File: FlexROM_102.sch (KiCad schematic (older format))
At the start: 5 parts, among them J1 27C256 DIP LEGS, U1 28C256

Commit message: footprint name changed
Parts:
- J1: footprint 000_LOCAL:DIP-28_W15.24mm_pcb_sil_pins -> 000_LOCAL:DIP28_0.6_pcb_sil_pins
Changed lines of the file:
@@
 F 0 "J1" H 4440 4190 50  0000 C CNN
 F 1 "27C256 DIP LEGS" H 4260 4420 50  0000 C CNN
-F 2 "000_LOCAL:DIP-28_W15.24mm_pcb_sil_pins" H 4260 3040 50  0001 C CNN
+F 2 "000_LOCAL:DIP28_0.6_pcb_sil_pins" H 4260 3040 50  0001 C CNN
 F 3 "http://ww1.microchip.com/downloads/en/DeviceDoc/doc0014.pdf" H 4260 3040 50  0001 C CNN
 	1    4260 3040

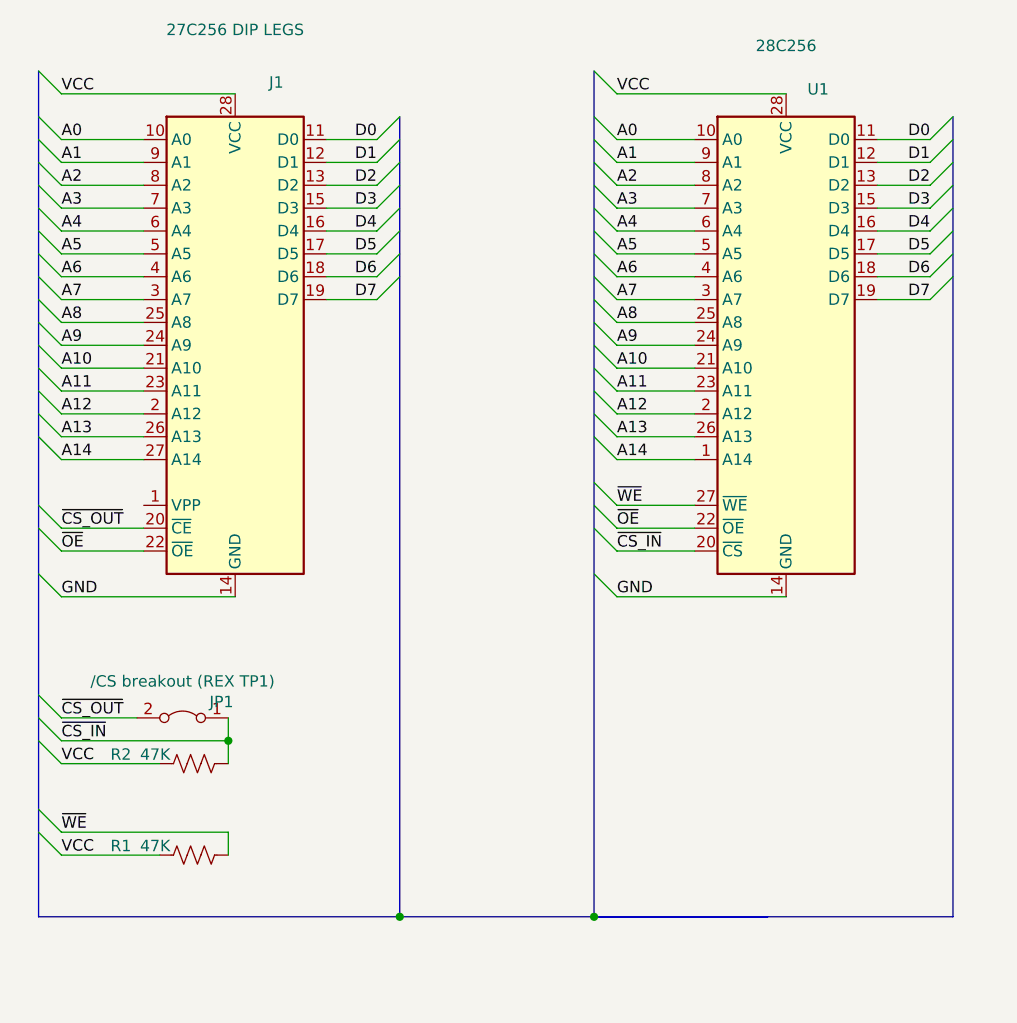
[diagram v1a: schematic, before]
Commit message: FlexROM_100 programming adapter, FlexROM_102 programming jumpers
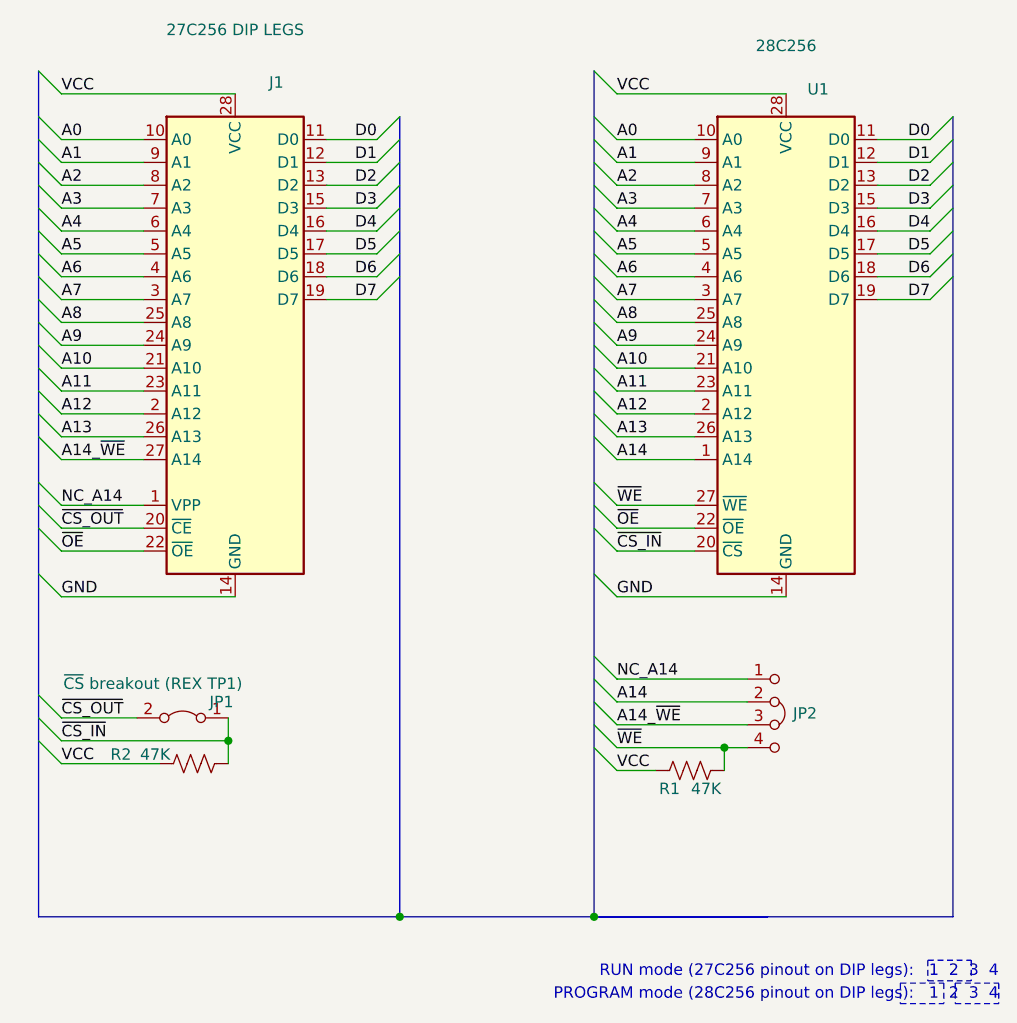
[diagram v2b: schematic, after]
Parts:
- added JP2: Jumper_4_Bridged23, Connector_PinHeader_2.00mm:PinHeader_1x04_P2.00mm_Horizontal, symbol 000_LOCAL:Jumper_4_Bridged23
- JP1: value /CS breakout (REX TP1) -> ~CS~ breakout (REX TP1)
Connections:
- net A14: now also JP2.2 (B); no longer J1.27 (A14)
- net ~WE: now also JP2.4 (D)
- net NC_A14: now reaches J1.1 (VPP)
- net NC_A14: now also JP2.1 (A)
- new net A14_~WE: J1.27 (A14), JP2.3 (C)
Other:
- note added: "PROGRAM mode (28C256 pinout on DIP legs): 1 2 3 4"
- note added: "RUN mode (27C256 pinout on DIP legs): 1 2 3 4"
- moved on the sheet: R1
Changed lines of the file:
@@
 A13
 Text Label 3500 3540 0    50   ~ 0
-A14
+A14_~WE
 Text Label 5930 2140 0    50   ~ 0
 A0
@@
 P 4030 4670
 F 0 "JP1" H 3860 4740 50  0000 C CNN
-F 1 "/CS breakout (REX TP1)" H 4030 4830 50  0000 C CNN
+F 1 "~CS~ breakout (REX TP1)" H 4160 4820 50  0000 C CNN
 F 2 "000_LOCAL:Pin_Header_Angled_1x02_Pitch2.54mm" H 4030 4670 50  0001 C CNN
 F 3 "~" H 4030 4670 50  0001 C CNN
@@
 Wire Bus Line
 	5830 5540 7400 5540
-Entry Wire Line
-	3400 5070 3500 5170
-Entry Wire Line
-	3400 5170 3500 5270
 $Comp
 L 000_LOCAL:R_US R1
 U 1 1 5E6B3AF8
-P 4080 5270
-F 0 "R1" V 4040 4950 50  0000 C CNN
-F 1 "47K" V 4040 5100 50  0000 C CNN
-F 2 "000_LOCAL:R_0805" H 4080 5270 50  0001 C CNN
-F 3 "~" H 4080 5270 50  0001 C CNN
-	1    4080 5270
+P 6250 4900
+F 0 "R1" V 6330 4810 50  0000 C CNN
+F 1 "47K" V 6330 4970 50  0000 C CNN
+F 2 "000_LOCAL:R_0805" H 6250 4900 50  0001 C CNN
+F 3 "~" H 6250 4900 50  0001 C CNN
+	1    6250 4900
 	0    1    1    0
 $EndComp
-Wire Wire Line
-	3500 5270 3930 5270
-Text Label 3500 5270 0    50   ~ 0
+Text Label 5930 4900 0    50   ~ 0
 VCC
-Text Label 3500 5170 0    50   ~ 0
+Text Label 5930 4800 0    50   ~ 0
 ~WE
 Connection ~ 4980 5540
@@
 Wire Wire Line
 	4230 4770 4230 4870
-Wire Wire Line
-	4230 5270 4230 5170
-Wire Wire Line
-	3500 5170 4230 5170
+Entry Wire Line
+	3400 3640 3500 3740
+Wire Wire Line
+	3860 3740 3500 3740
+Text Label 3500 3740 0    50   ~ 0
+NC_A14
+Entry Wire Line
+	5830 4400 5930 4500
+Entry Wire Line
+	5830 4500 5930 4600
+Entry Wire Line
+	5830 4600 5930 4700
+Entry Wire Line
+	5830 4700 5930 4800
+Entry Wire Line
+	5830 4800 5930 4900
+Wire Wire Line
+	5930 4900 6100 4900
+Wire Wire Line
+	5930 4800 6400 4800
+Wire Wire Line
+	6400 4800 6400 4900
+Wire Wire Line
+	6400 4800 6500 4800
+Connection ~ 6400 4800
+Wire Wire Line
+	5930 4700 6500 4700
+Wire Wire Line
+	5930 4600 6500 4600
+Wire Wire Line
+	5930 4500 6500 4500
+Text Label 5930 4700 0    50   ~ 0
+A14_~WE
+Text Label 5930 4600 0    50   ~ 0
+A14
+Text Label 5930 4500 0    50   ~ 0
+NC_A14
+$Comp
+L 000_LOCAL:Jumper_4_Bridged23 JP2
+U 1 1 5FA17830
+P 6750 4500
+F 0 "JP2" H 6700 4350 50  0000 L CNN
+F 1 "Jumper_4_Bridged23" H 6700 4300 50  0001 L CNN
+F 2 "Connector_PinHeader_2.00mm:PinHeader_1x04_P2.00mm_Horizontal" H 6750 4500 50  0001 C CNN
+F 3 "~" H 6750 4500 50  0001 C CNN
+	1    6750 4500
+	1    0    0    -1
+$EndComp
+Text Notes 7600 5810 2    50   ~ 0
+RUN mode (27C256 pinout on DIP legs):   1  2  3  4
+Text Notes 7600 5910 2    50   ~ 0
+PROGRAM mode (28C256 pinout on DIP legs):   1  2  3  4
+Wire Notes Line style solid
+	7410 5830 7410 5920
+Wire Notes Line style solid
+	7600 5830 7600 5920
+Wire Notes Line style solid
+	7410 5830 7600 5830
+Wire Notes Line style solid
+	7410 5920 7600 5920
+Wire Notes Line style solid
+	7290 5730 7290 5820
+Wire Notes Line style solid
+	7480 5730 7480 5820
+Wire Notes Line style solid
+	7290 5730 7480 5730
+Wire Notes Line style solid
+	7290 5820 7480 5820
+Wire Notes Line style solid
+	7170 5830 7170 5920
+Wire Notes Line style solid
+	7360 5830 7360 5920
+Wire Notes Line style solid
+	7170 5830 7360 5830
+Wire Notes Line style solid
+	7170 5920 7360 5920
 Wire Bus Line
 	4980 2040 4980 5540

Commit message: silkscreen
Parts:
- JP2: footprint Connector_PinHeader_2.00mm:PinHeader_1x04_P2.00mm_Horizontal -> 000_LOCAL:PinHeader_1x04_P2.00mm_Horizontal
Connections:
- net A14: now also JP2.3 (C); no longer JP2.2 (B)
- net A14_~WE: now also JP2.2 (B); no longer JP2.3 (C)
- net NC_A14: now also JP2.4 (D); no longer JP2.1 (A)
- net ~WE: now also JP2.1 (A); no longer JP2.4 (D)
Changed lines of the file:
@@
 L 000_LOCAL:Jumper_4_Bridged23 JP2
 U 1 1 5FA17830
-P 6750 4500
-F 0 "JP2" H 6700 4350 50  0000 L CNN
-F 1 "Jumper_4_Bridged23" H 6700 4300 50  0001 L CNN
-F 2 "Connector_PinHeader_2.00mm:PinHeader_1x04_P2.00mm_Horizontal" H 6750 4500 50  0001 C CNN
-F 3 "~" H 6750 4500 50  0001 C CNN
-	1    6750 4500
-	1    0    0    -1
+P 6750 4800
+F 0 "JP2" H 6700 4650 50  0000 L CNN
+F 1 "Jumper_4_Bridged23" H 6700 4600 50  0001 L CNN
+F 2 "000_LOCAL:PinHeader_1x04_P2.00mm_Horizontal" H 6750 4800 50  0001 C CNN
+F 3 "~" H 6750 4800 50  0001 C CNN
+	1    6750 4800
+	1    0    0    1
 $EndComp
 Text Notes 7600 5810 2    50   ~ 0

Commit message: add model 100 optrom programming adapter. readme and renders
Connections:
- net VCC: now also R1.1; no longer R1.2
- net ~WE: now also R1.2; no longer R1.1
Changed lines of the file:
@@
 F 3 "~" H 6250 4900 50  0001 C CNN
 	1    6250 4900
-	0    1    1    0
+	0    -1   1    0
 $EndComp
 Text Label 5930 4900 0    50   ~ 0
